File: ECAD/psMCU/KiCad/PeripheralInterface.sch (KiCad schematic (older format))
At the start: 7 parts, among them J6 PERIPH_INTERFACE, U349 SN74LVC1G08DCK, U350 SN74LVC1G08DCK, U351 SN74LVC1G08DCK

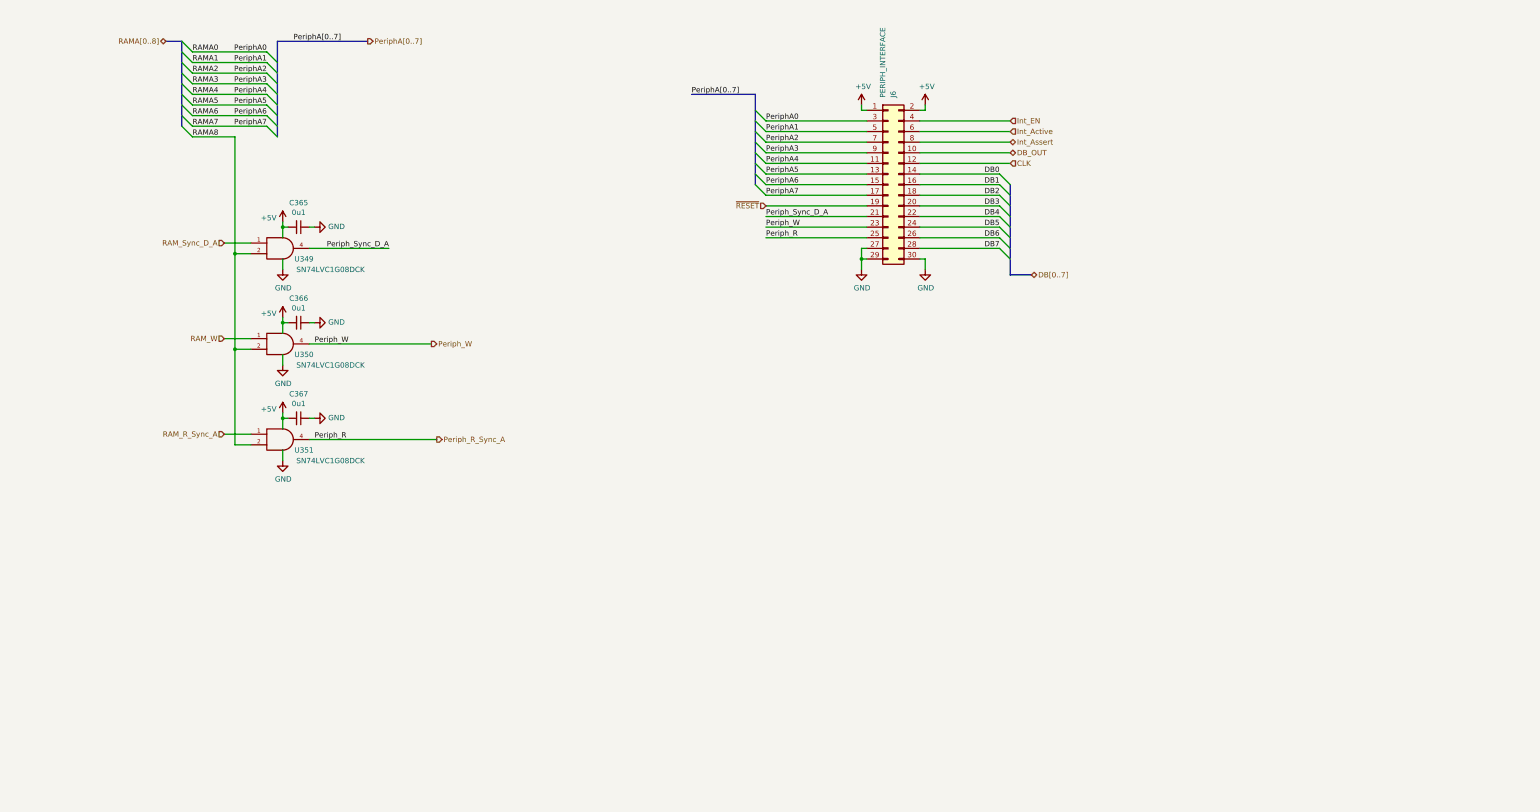
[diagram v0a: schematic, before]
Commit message: Sch: Reworked Peripheral Interface (Buffers)
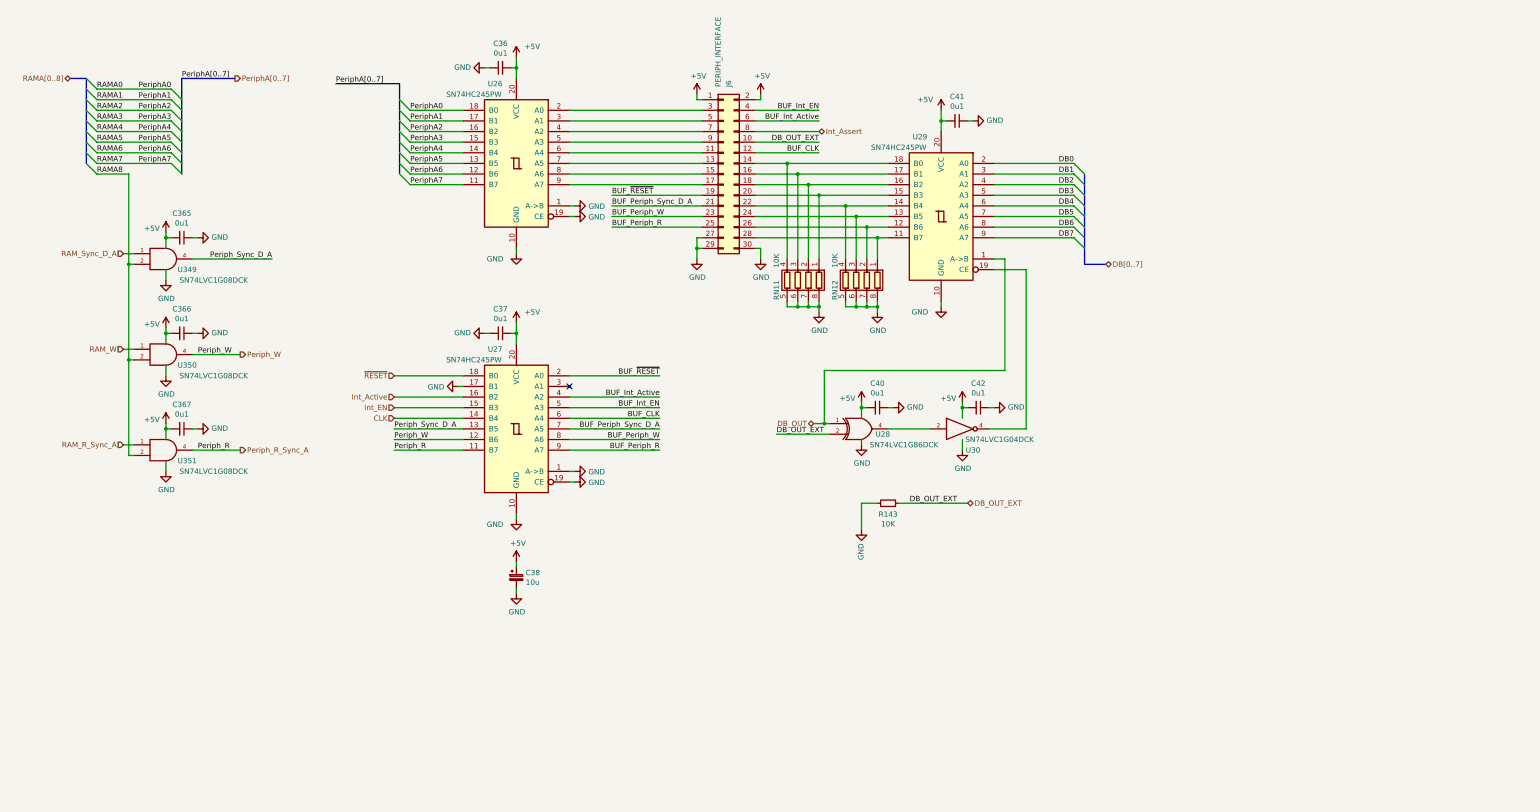
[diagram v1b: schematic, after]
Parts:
- added C36, C37, C40, C41, C42: 0u1, NoRef_Footprints:C_0603_1608Metric_NoRef, symbol Device:C_Small
- added C38: 10u, symbol Device:CP_Small
- added R143: 10K, NoRef_Footprints:R_0603_1608Metric_NoRef, symbol Device:R_Small
- added RN11, RN12: 10K, NoRef_Footprints:R_Array_Convex_4x0603_NoRef, symbol Device:R_Pack04
- added U26, U27, U29: SN74HC245PW, Package_SO:TSSOP-20_4.4x6.5mm_P0.65mm, symbol 74xx:74HC245
- added U28: SN74LVC1G86DCK, Package_TO_SOT_SMD:SOT-353_SC-70-5, symbol 74xGxx:74LVC1G86
- added U30: SN74LVC1G04DCK, Package_TO_SOT_SMD:SOT-353_SC-70-5, symbol 74xGxx:74LVC1G04
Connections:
- net +5V: now also C36.2, C37.2, C38.1, C40.2, C41.2, C42.2, U26.20 (VCC), U27.20 (VCC), U28.5 (VCC), U29.20 (VCC), U30.5 (VCC)
- net CLK: now also U27.14 (B4); no longer J6.12 (Pin_12)
- net DB0: now also U29.2 (A0); no longer J6.14 (Pin_14)
- net DB1: now also U29.3 (A1); no longer J6.16 (Pin_16)
- net DB2: now also U29.4 (A2); no longer J6.18 (Pin_18)
- net DB3: now also U29.5 (A3); no longer J6.20 (Pin_20)
- net DB4: now also U29.6 (A4); no longer J6.22 (Pin_22)
- net DB5: now also U29.7 (A5); no longer J6.24 (Pin_24)
- net DB6: now also U29.8 (A6); no longer J6.26 (Pin_26)
- net DB7: now also U29.9 (A7); no longer J6.28 (Pin_28)
- net DB_OUT: now also U28.1, U29.1 (A->B); no longer J6.10 (Pin_10)
- net GND: now also C36.1, C37.1, C38.2, C40.1, C41.1, C42.1, R143.2, RN11.5 (R4.2), RN11.6 (R3.2), RN11.7 (R2.2), RN11.8 (R1.2), RN12.5 (R4.2), RN12.6 (R3.2), RN12.7 (R2.2), RN12.8 (R1.2), U26.1 (A->B), U26.10 (GND), U26.19 (CE), U27.1 (A->B), U27.10 (GND), U27.17 (B1), U27.19 (CE), U28.3 (GND), U29.10 (GND), U30.3 (GND)
- net Int_Active: now also U27.16 (B2); no longer J6.6 (Pin_6)
- net Int_EN: now also U27.15 (B3); no longer J6.4 (Pin_4)
- net PeriphA0: now also U26.18 (B0); no longer J6.3 (Pin_3)
- net PeriphA1: now also U26.17 (B1); no longer J6.5 (Pin_5)
- net PeriphA2: now also U26.16 (B2); no longer J6.7 (Pin_7)
- net PeriphA3: now also U26.15 (B3); no longer J6.9 (Pin_9)
- net PeriphA4: now also U26.14 (B4); no longer J6.11 (Pin_11)
- net PeriphA5: now also U26.13 (B5); no longer J6.13 (Pin_13)
- net PeriphA6: now also U26.12 (B6); no longer J6.15 (Pin_15)
- net PeriphA7: now also U26.11 (B7); no longer J6.17 (Pin_17)
- net Periph_R_Sync_A: now also U27.11 (B7); no longer J6.25 (Pin_25)
- net Periph_Sync_D_A: now also U27.13 (B5); no longer J6.21 (Pin_21)
- net Periph_W: now also U27.12 (B6); no longer J6.23 (Pin_23)
- net ~RESET: now also U27.18 (B0); no longer J6.19 (Pin_19)
- new net: J6.11 (Pin_11), U26.6 (A4)
- new net: J6.13 (Pin_13), U26.7 (A5)
- new net: J6.14 (Pin_14), RN11.4 (R4.1), U29.18 (B0)
- new net: J6.15 (Pin_15), U26.8 (A6)
- new net: J6.16 (Pin_16), RN11.3 (R3.1), U29.17 (B1)
- new net: J6.17 (Pin_17), U26.9 (A7)
- new net: J6.18 (Pin_18), RN11.2 (R2.1), U29.16 (B2)
- new net: J6.20 (Pin_20), RN11.1 (R1.1), U29.15 (B3)
- new net: J6.22 (Pin_22), RN12.4 (R4.1), U29.14 (B4)
- new net: J6.24 (Pin_24), RN12.3 (R3.1), U29.13 (B5)
- new net: J6.26 (Pin_26), RN12.2 (R2.1), U29.12 (B6)
- new net: J6.28 (Pin_28), RN12.1 (R1.1), U29.11 (B7)
- new net: J6.3 (Pin_3), U26.2 (A0)
- new net: J6.5 (Pin_5), U26.3 (A1)
- new net: J6.7 (Pin_7), U26.4 (A2)
- new net: J6.9 (Pin_9), U26.5 (A3)
- new net: U29.19 (CE), U30.4
- new net: U28.4, U30.2
- new net BUF_CLK: J6.12 (Pin_12), U27.6 (A4)
- new net BUF_Int_Active: J6.6 (Pin_6), U27.4 (A2)
- new net BUF_Int_EN: J6.4 (Pin_4), U27.5 (A3)
- new net BUF_Periph_R: J6.25 (Pin_25), U27.9 (A7)
- new net BUF_Periph_Sync_D_A: J6.21 (Pin_21), U27.7 (A5)
- new net BUF_Periph_W: J6.23 (Pin_23), U27.8 (A6)
- new net BUF_~RESET: J6.19 (Pin_19), U27.2 (A0)
- new net DB_OUT_EXT: J6.10 (Pin_10), R143.1, U28.2
- no-connect marks 0 -> 1
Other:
- moved on the sheet: C365, C366, C367, J6, U349, U350, U351

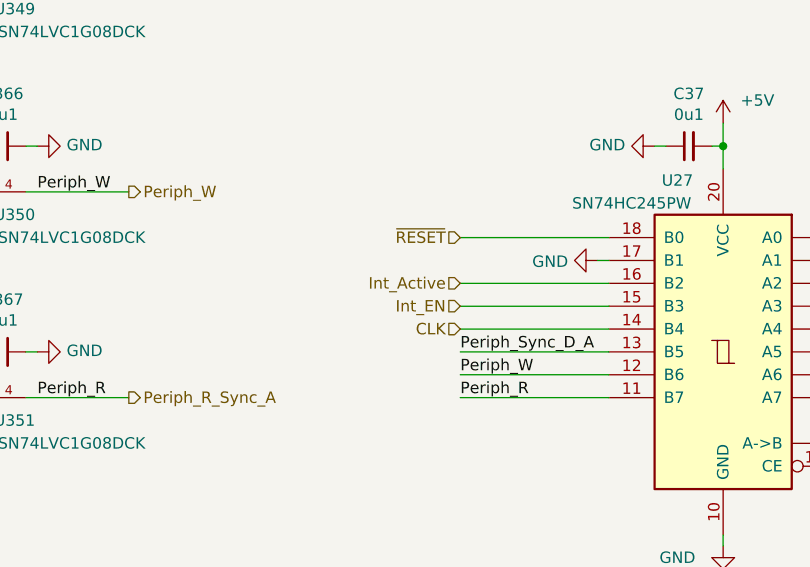
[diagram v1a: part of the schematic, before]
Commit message: Sch: Improved Clk/Reset distribution, moved to global labels
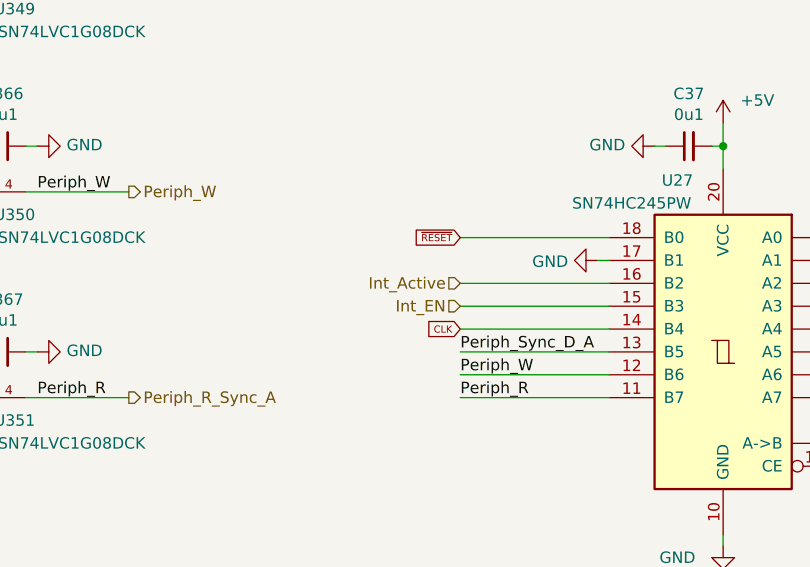
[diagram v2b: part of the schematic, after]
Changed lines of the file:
@@
 $Descr A4 11693 8268
 encoding utf-8
-Sheet 41 96
+Sheet 39 97
 Title "psMCU"
 Date "2022-02-13"
@@
 Text HLabel 10800 2900 2    50   3State ~ 0
 DB[0..7]
-Text HLabel 4100 4350 0    50   Input ~ 0
-CLK
 Text HLabel 1550 2800 0    50   Input ~ 0
 RAM_Sync_D_A
@@
 	1    0    0    -1
 $EndComp
-Text HLabel 4100 3950 0    50   Input ~ 0
-~RESET
 Wire Wire Line
 	4100 3950 4750 3950
@@
 Wire Wire Line
 	10050 4450 10050 2950
+Text GLabel 4100 4350 0    31   Input ~ 0
+CLK
+Text GLabel 4100 3950 0    31   Input ~ 0
+~RESET
 Wire Bus Line
 	4150 1200 4150 2050

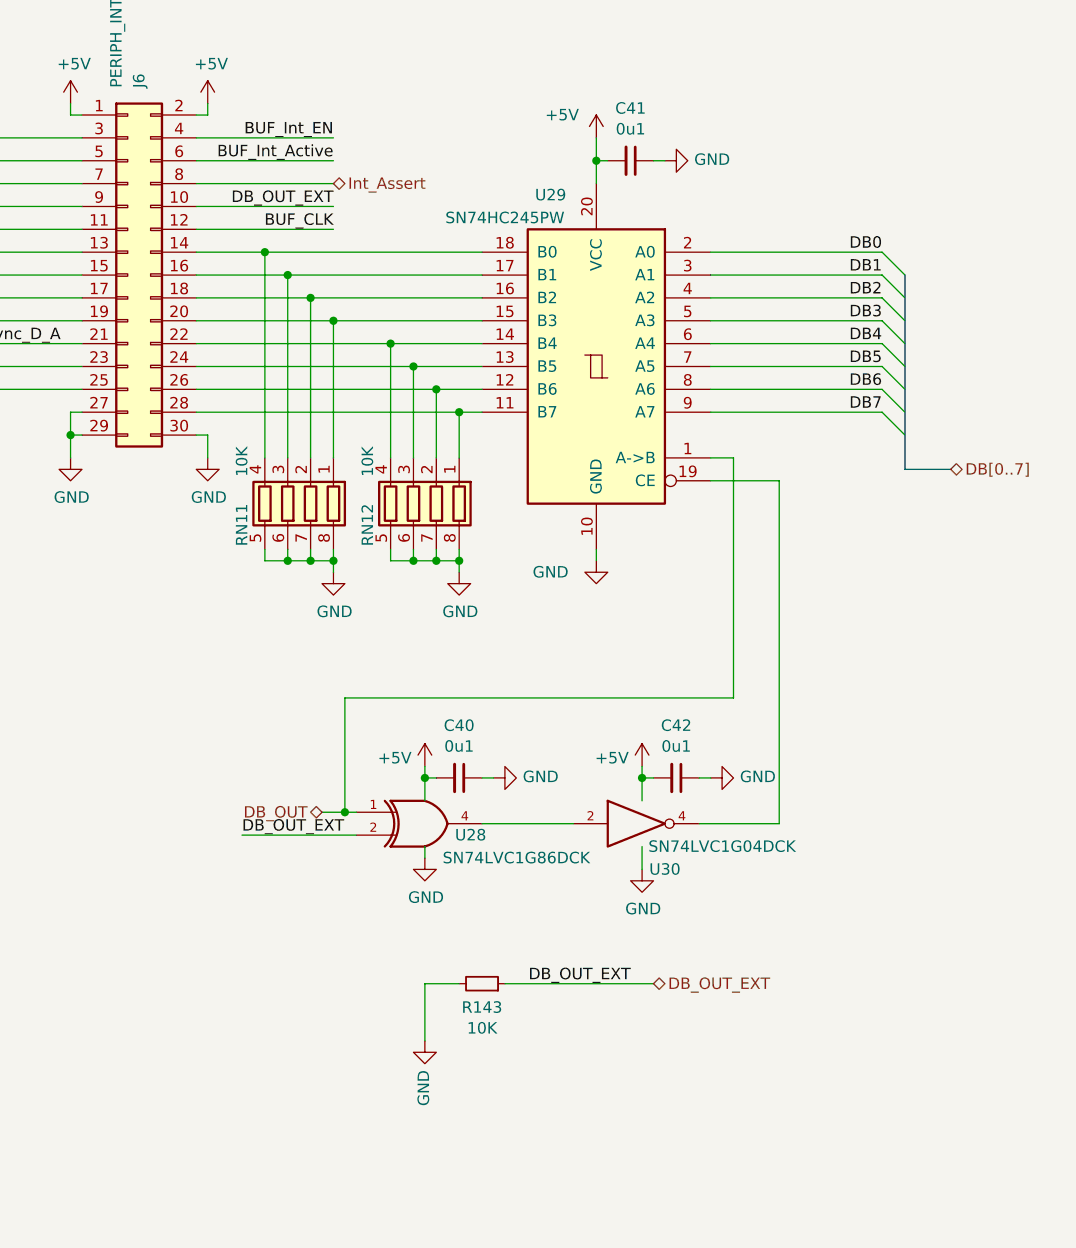
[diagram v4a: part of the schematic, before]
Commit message: Sch: Addded Buffer for external interrupt assert
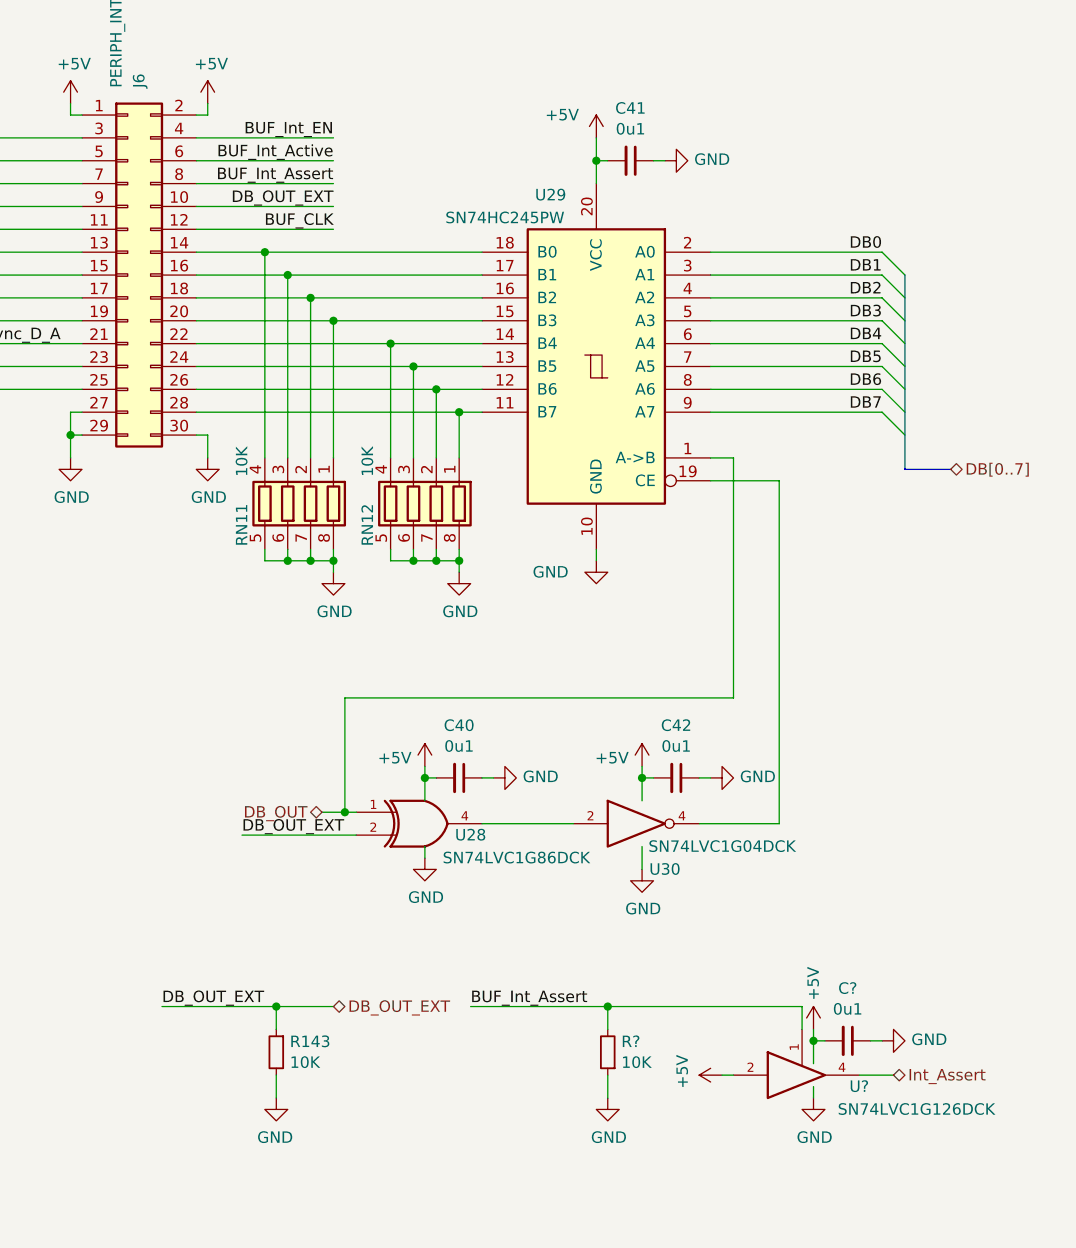
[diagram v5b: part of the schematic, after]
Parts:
- added C?: 0u1, NoRef_Footprints:C_0603_1608Metric_NoRef, symbol Device:C_Small
- added R?: 10K, NoRef_Footprints:R_0603_1608Metric_NoRef, symbol Device:R_Small
- added U?: SN74LVC1G126DCK, Package_TO_SOT_SMD:SOT-353_SC-70-5, symbol 74xGxx:74LVC1G126
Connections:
- net +5V: now also C?.2, U?.2, U?.5 (VCC)
- net GND: now also C?.1, R?.1, U?.3 (GND)
- net Int_Assert: now also U?.4; no longer J6.8 (Pin_8)
- new net BUF_Int_Assert: J6.8 (Pin_8), R?.2, U?.1
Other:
- moved on the sheet: R143
